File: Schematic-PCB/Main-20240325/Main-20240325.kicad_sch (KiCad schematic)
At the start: 104 parts, among them J1 Conn_01x10_Pin, J2 Conn_01x03_Pin, J3 Conn_01x15_Pin, J4 Conn_02x05_Odd_Even, U1 DEV-16771, U10 TSSP58038, U11 TSSP58038, U12 TSSP58038, U13 TSSP58038, U14 TSSP58038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

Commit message: 回路/基板をいろいろ直した
具体的にはあんまり進んでないけど
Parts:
- removed JP2, JP4: Jumper_2_Small_Open, Jumper:SolderJumper-2_P1.3mm_Open_Pad1.0x1.5mm, symbol Jumper:Jumper_2_Small_Open
- added D19: D_Small, symbol Device:D_Small
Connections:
- net SW-TAC-5 is gone; now on net KickerSignal: J1.7 (Pin_7), U1.32 (OUT1B)
- net +5V: now also D19.2 (A); no longer U2.14 (5V)
- net SW-TAC-3: now also U1.31 (CTX3); no longer U1.35 (TX8)
- net SW-TAC-4: now also U1.30 (CRX3); no longer U1.34 (RX8)
- net at R5.2: now also U2.9 (SCK_D8); no longer U2.8 (RX_D7)
- net Main-RX2: now reaches U2.7 (TX_D6)
- net Main-RX2: now also U1.7 (RX2)
- net Cam-main=RX renamed Cam-TX
- net Cam-TX: now also U1.34 (RX8); no longer U1.7 (RX2)
- net Cam-main=TX renamed Cam-RX
- net Cam-RX: now also U1.35 (TX8); no longer U1.8 (TX2)
- net Cam_MISO_RX renamed Cam-MISO_RX
- net Cam_MOSI_TX renamed Cam-MOSI_TX
- net KickerSignal-main renamed KickerSignal
- net KickerSignal: no longer U1.30 (CRX3)
- net Line-MD-Main=RX_3.3V renamed Line-TX
- net Line-MD-Main=TX_3.3V renamed Line-RX
- new net: D19.1 (K), U2.14 (5V)
- new net Main-TX2: U1.8 (TX2), U2.8 (RX_D7)
- no-connect marks 27 -> 26
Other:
- note added: "UART"
- moved on the sheet: C1, C10, C11, C12, C13, C14, C15, C16, C17, C18, C19, C2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

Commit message: MDのDRしたよ
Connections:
- net KickerSignal: now also J3.10 (Pin_10); no longer J3.11 (Pin_11)
- net ball02k: now also J3.11 (Pin_11); no longer J3.10 (Pin_10)

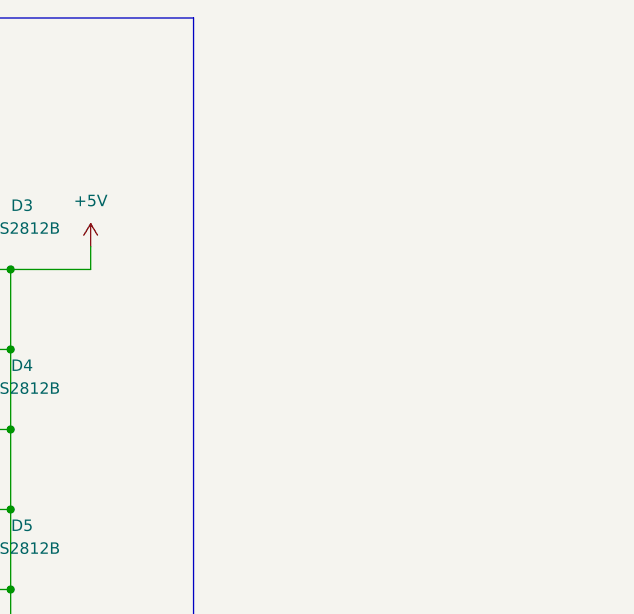
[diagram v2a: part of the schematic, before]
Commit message: ドリブラー用のコネクタを追加した
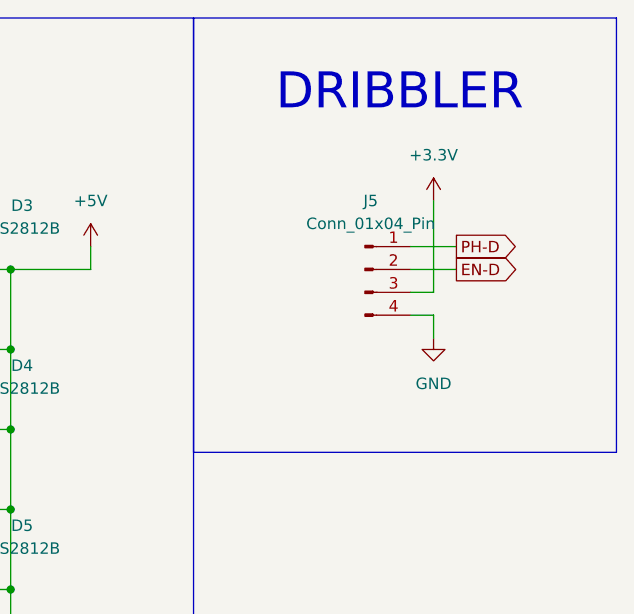
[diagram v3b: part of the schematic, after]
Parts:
- added J5: Conn_01x04_Pin, symbol Connector:Conn_01x04_Pin
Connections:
- net +3.3V: now also J5.3 (Pin_3)
- net GND: now also J5.4 (Pin_4)
- new net EN-D: J5.2 (Pin_2)
- new net PH-D: J5.1 (Pin_1)
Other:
- note added: "DRIBBLER"

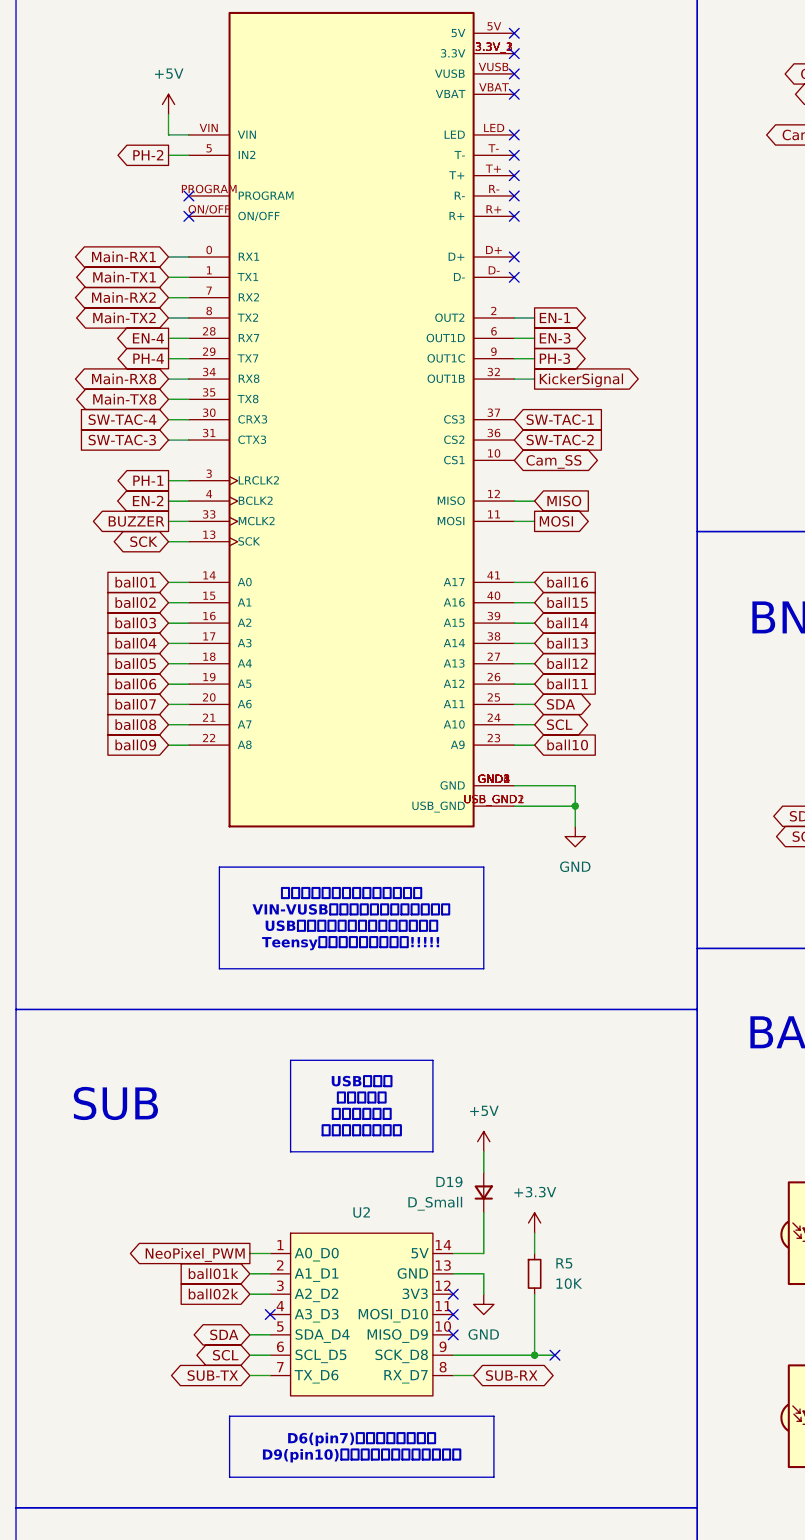
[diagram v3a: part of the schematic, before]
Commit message: メイン基板の部品を仮で配置したよ
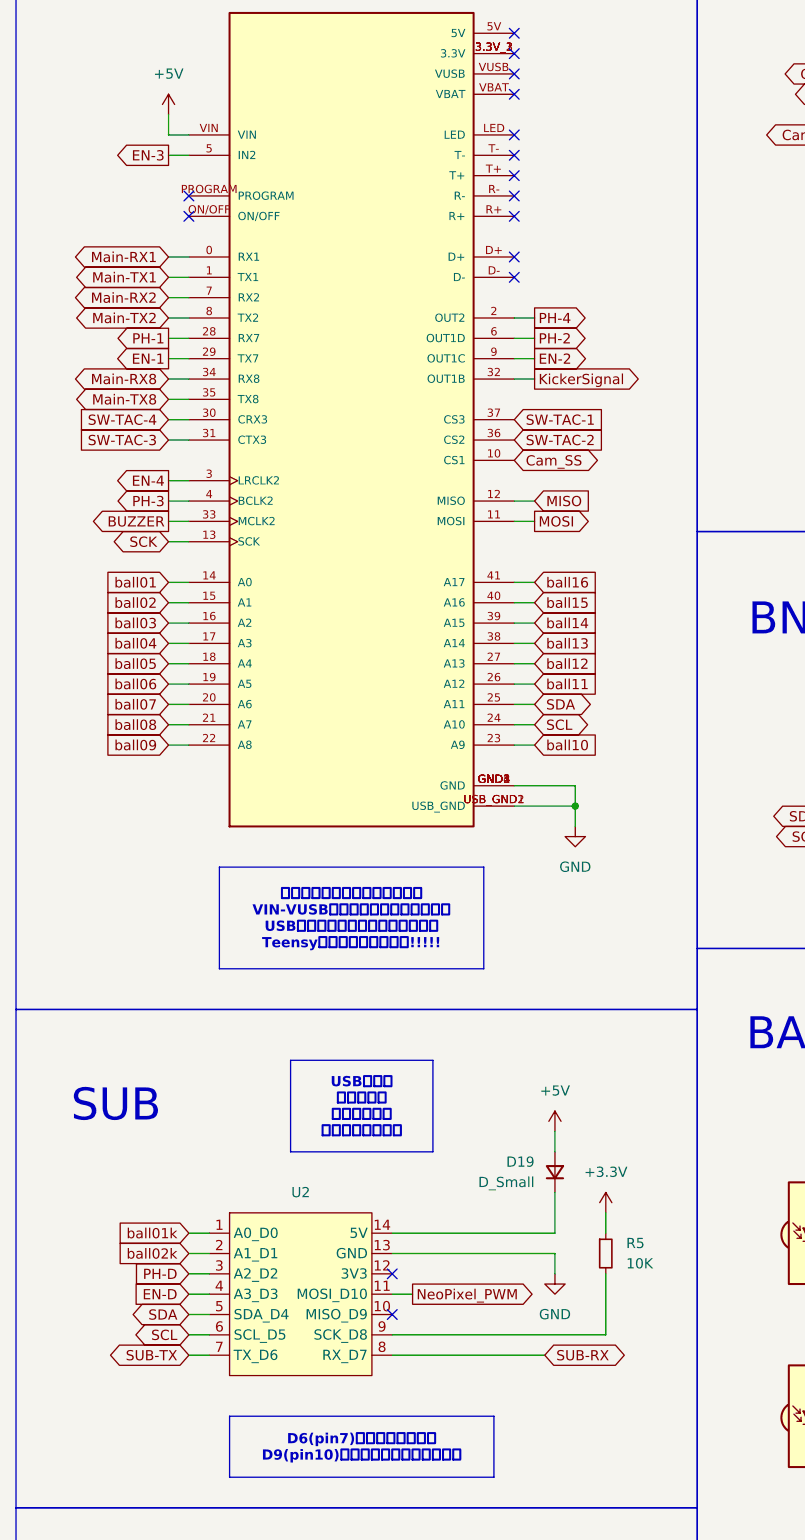
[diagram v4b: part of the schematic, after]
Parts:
- D19: footprint (none) -> Diode_THT:D_A-405_P7.62mm_Horizontal
- J5: footprint (none) -> Connector_JST:JST_XH_B4B-XH-A_1x04_P2.50mm_Vertical
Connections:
- net EN-1: now also U1.29 (TX7); no longer U1.2 (OUT2)
- net EN-2: now also U1.9 (OUT1C); no longer U1.4 (BCLK2)
- net EN-3: now also U1.5 (IN2); no longer U1.6 (OUT1D)
- net EN-4: now also U1.3 (LRCLK2); no longer U1.28 (RX7)
- net EN-D: now also U2.4 (A3_D3)
- net NeoPixel_PWM: now also U2.11 (MOSI_D10); no longer U2.1 (A0_D0)
- net PH-1: now also U1.28 (RX7); no longer U1.3 (LRCLK2)
- net PH-2: now also U1.6 (OUT1D); no longer U1.5 (IN2)
- net PH-3: now also U1.4 (BCLK2); no longer U1.9 (OUT1C)
- net PH-4: now also U1.2 (OUT2); no longer U1.29 (TX7)
- net PH-D: now also U2.3 (A2_D2)
- net ball01k: now also U2.1 (A0_D0); no longer U2.2 (A1_D1)
- net ball02k: now also U2.2 (A1_D1); no longer U2.3 (A2_D2)
- no-connect marks 26 -> 23
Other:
- moved on the sheet: D19, R5, U2

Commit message: BNO055のフットプリントを修正した
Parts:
- U1: footprint @2024-Main:MODULE_DEV-16771 -> @2024TOINIOT2-Main:MODULE_DEV-16771
- U10, U11, U12, U13, U14, U15, U16, U17, U18, U19, U4, U5, U6, U7, U8, U9: footprint @2024-Main:Vishay_MINICAST-3Pin -> @2024TOINIOT2-Main:Vishay_MINICAST-3Pin
- U2: footprint @2024-Main:XIAO ESP32C3 -> @2024TOINIOT2-Main:XIAO ESP32C3
- U3: footprint Package_DIP:DIP-8_W7.62mm -> @2024TOINIOT2-Main:BNO055
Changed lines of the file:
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@@
 			)
 		)
-		(property "Footprint" "@2024-Main:Vishay_MINICAST-3Pin"
+		(property "Footprint" "@2024TOINIOT2-Main:Vishay_MINICAST-3Pin"
 			(at 166.37 235.585 0)
 			(effects
@@
 			)
 		)
-		(property "Footprint" "@2024-Main:XIAO ESP32C3"
+		(property "Footprint" "@2024TOINIOT2-Main:XIAO ESP32C3"
 			(at 48.26 169.672 0)
 			(effects
@@
 			)
 		)
-		(property "Footprint" "@2024-Main:Vishay_MINICAST-3Pin"
+		(property "Footprint" "@2024TOINIOT2-Main:Vishay_MINICAST-3Pin"
 			(at 166.37 189.865 0)
 			(effects
@@
 			)
 		)
-		(property "Footprint" "@2024-Main:Vishay_MINICAST-3Pin"
+		(property "Footprint" "@2024TOINIOT2-Main:Vishay_MINICAST-3Pin"
 			(at 118.11 349.885 0)
 			(effects
@@
 			)
 		)
-		(property "Footprint" "@2024-Main:Vishay_MINICAST-3Pin"
+		(property "Footprint" "@2024TOINIOT2-Main:Vishay_MINICAST-3Pin"
 			(at 166.37 304.165 0)
 			(effects
@@
 			)
 		)
-		(property "Footprint" "Package_DIP:DIP-8_W7.62mm"
+		(property "Footprint" "@2024TOINIOT2-Main:BNO055"
 			(at 139.7 118.364 0)
 			(effects
@@
 			)
 		)
-		(property "Footprint" "@2024-Main:Vishay_MINICAST-3Pin"
+		(property "Footprint" "@2024TOINIOT2-Main:Vishay_MINICAST-3Pin"
 			(at 166.37 349.885 0)
 			(effects
@@
 			)
 		)
-		(property "Footprint" "@2024-Main:Vishay_MINICAST-3Pin"
+		(property "Footprint" "@2024TOINIOT2-Main:Vishay_MINICAST-3Pin"
 			(at 118.11 189.865 0)
 			(effects
@@
 			)
 		)
-		(property "Footprint" "@2024-Main:Vishay_MINICAST-3Pin"
+		(property "Footprint" "@2024TOINIOT2-Main:Vishay_MINICAST-3Pin"
 			(at 118.11 258.445 0)
 			(effects
@@
 			)
 		)
-		(property "Footprint" "@2024-Main:Vishay_MINICAST-3Pin"
+		(property "Footprint" "@2024TOINIOT2-Main:Vishay_MINICAST-3Pin"
 			(at 118.11 235.585 0)
 			(effects
@@
 			)
 		)
-		(property "Footprint" "@2024-Main:Vishay_MINICAST-3Pin"
+		(property "Footprint" "@2024TOINIOT2-Main:Vishay_MINICAST-3Pin"
 			(at 166.37 327.025 0)
 			(effects
@@
 			)
 		)
-		(property "Footprint" "@2024-Main:MODULE_DEV-16771"
+		(property "Footprint" "@2024TOINIOT2-Main:MODULE_DEV-16771"
 			(at 54.61 78.74 0)
 			(effects
@@
 			)
 		)
-		(property "Footprint" "@2024-Main:Vishay_MINICAST-3Pin"
+		(property "Footprint" "@2024TOINIOT2-Main:Vishay_MINICAST-3Pin"
 			(at 166.37 281.305 0)
 			(effects
@@
 			)
 		)
-		(property "Footprint" "@2024-Main:Vishay_MINICAST-3Pin"
+		(property "Footprint" "@2024TOINIOT2-Main:Vishay_MINICAST-3Pin"
 			(at 118.11 304.165 0)
 			(effects
@@
 			)
 		)
-		(property "Footprint" "@2024-Main:Vishay_MINICAST-3Pin"
+		(property "Footprint" "@2024TOINIOT2-Main:Vishay_MINICAST-3Pin"
 			(at 166.37 258.445 0)
 			(effects
@@
 			)
 		)
-		(property "Footprint" "@2024-Main:Vishay_MINICAST-3Pin"
+		(property "Footprint" "@2024TOINIOT2-Main:Vishay_MINICAST-3Pin"
 			(at 118.11 212.725 0)
 			(effects
@@
 			)
 		)
-		(property "Footprint" "@2024-Main:Vishay_MINICAST-3Pin"
+		(property "Footprint" "@2024TOINIOT2-Main:Vishay_MINICAST-3Pin"
 			(at 118.11 281.305 0)
 			(effects
@@
 			)
 		)
-		(property "Footprint" "@2024-Main:Vishay_MINICAST-3Pin"
+		(property "Footprint" "@2024TOINIOT2-Main:Vishay_MINICAST-3Pin"
 			(at 166.37 212.725 0)
 			(effects
@@
 			)
 		)
-		(property "Footprint" "@2024-Main:Vishay_MINICAST-3Pin"
+		(property "Footprint" "@2024TOINIOT2-Main:Vishay_MINICAST-3Pin"
 			(at 118.11 327.025 0)
 			(effects

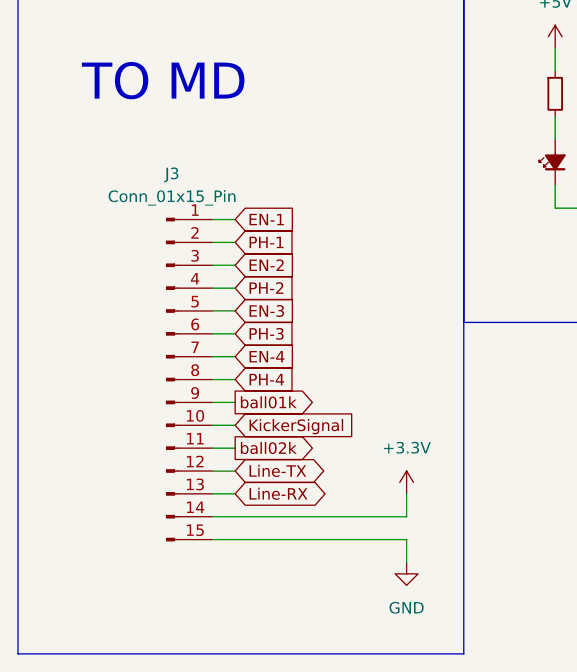
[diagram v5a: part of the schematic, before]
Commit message: メイン基板のPCBを更新した
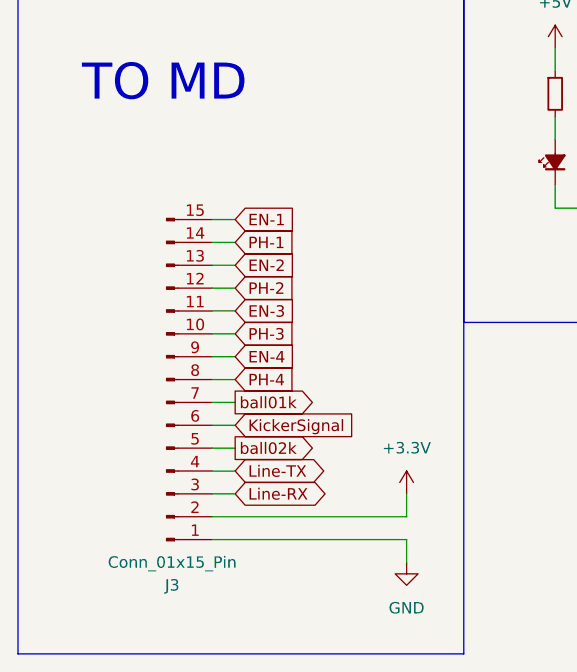
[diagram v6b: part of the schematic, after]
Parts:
- J3: footprint Connector_FFC-FPC:TE_1-1734839-5_1x15-1MP_P0.5mm_Horizontal -> @2024-MD:1.0K-FX-15PWB
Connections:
- net +3.3V: now also J3.2 (Pin_2); no longer J3.14 (Pin_14)
- net EN-1: now also J3.15 (Pin_15); no longer J3.1 (Pin_1)
- net EN-2: now also J3.13 (Pin_13); no longer J3.3 (Pin_3)
- net EN-3: now also J3.11 (Pin_11); no longer J3.5 (Pin_5)
- net EN-4: now also J3.9 (Pin_9); no longer J3.7 (Pin_7)
- net GND: now also J3.1 (Pin_1); no longer J3.15 (Pin_15)
- net KickerSignal: now also J3.6 (Pin_6); no longer J3.10 (Pin_10)
- net Line-RX: now also J3.3 (Pin_3); no longer J3.13 (Pin_13)
- net Line-TX: now also J3.4 (Pin_4); no longer J3.12 (Pin_12)
- net PH-1: now also J3.14 (Pin_14); no longer J3.2 (Pin_2)
- net PH-2: now also J3.12 (Pin_12); no longer J3.4 (Pin_4)
- net PH-3: now also J3.10 (Pin_10); no longer J3.6 (Pin_6)
- net ball01k: now also J3.7 (Pin_7); no longer J3.9 (Pin_9)
- net ball02k: now also J3.5 (Pin_5); no longer J3.11 (Pin_11)
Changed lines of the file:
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@@
 		(lib_id "Connector:Conn_01x15_Pin")
 		(at 29.21 368.3 0)
+		(mirror x)
 		(unit 1)
 		(exclude_from_sim no)
@@
 		(dnp no)
 		(property "Reference" "J3"
-			(at 29.845 345.44 0)
+			(at 29.845 391.16 0)
 			(effects
 				(font
@@
 		)
 		(property "Value" "Conn_01x15_Pin"
-			(at 29.845 347.98 0)
+			(at 29.845 388.62 0)
 			(effects
 				(font
@@
 			)
 		)
-		(property "Footprint" "Connector_FFC-FPC:TE_1-1734839-5_1x15-1MP_P0.5mm_Horizontal"
+		(property "Footprint" "@2024-MD:1.0K-FX-15PWB"
 			(at 29.21 368.3 0)
 			(effects
